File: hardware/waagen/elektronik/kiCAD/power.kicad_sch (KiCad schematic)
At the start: 7 parts, among them U2 MCP1700-3302E_TO92

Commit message: fues added and small movements
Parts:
- added F1: Polyfuse 500mA, Resistor_SMD:R_1206_3216Metric_Pad1.30x1.75mm_HandSolder, symbol Device:Polyfuse
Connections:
- net +9V: now also F1.1; no longer C7.1, U2.2 (VI)
- new net: C7.1, F1.2, U2.2 (VI)
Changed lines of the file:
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@@
 (kicad_sch (version 20211123) (generator eeschema)
   (paper "A4")
+  (junction (at 111.76 91.44) (diameter 0) (color 0 0 0 0)
+  )
+  (junction (at 93.98 91.44) (diameter 0) (color 0 0 0 0)
+  )
   (junction (at 138.43 91.44) (diameter 0) (color 0 0 0 0)
   )
-  (junction (at 111.76 91.44) (diameter 0) (color 0 0 0 0)
-  )
-  (junction (at 93.98 91.44) (diameter 0) (color 0 0 0 0)
+  (junction (at 148.59 91.44) (diameter 0) (color 0 0 0 0)
   )
   (junction (at 102.87 91.44) (diameter 0) (color 0 0 0 0)
@@
     (stroke (width 0) (type default) (color 0 0 0 0))
   )
+  (wire (pts (xy 219.71 105.41) (xy 219.71 106.68))
+    (stroke (width 0) (type default) (color 0 0 0 0))
+  )
+  (wire (pts (xy 138.43 99.06) (xy 138.43 102.87))
+    (stroke (width 0) (type default) (color 0 0 0 0))
+  )
+  (wire (pts (xy 125.73 99.06) (xy 125.73 102.87))
+    (stroke (width 0) (type default) (color 0 0 0 0))
+  )
   (wire (pts (xy 133.35 91.44) (xy 138.43 91.44))
     (stroke (width 0) (type default) (color 0 0 0 0))
   )
-  (wire (pts (xy 219.71 105.41) (xy 219.71 106.68))
-    (stroke (width 0) (type default) (color 0 0 0 0))
-  )
-  (wire (pts (xy 138.43 99.06) (xy 138.43 102.87))
-    (stroke (width 0) (type default) (color 0 0 0 0))
-  )
-  (wire (pts (xy 125.73 99.06) (xy 125.73 102.87))
-    (stroke (width 0) (type default) (color 0 0 0 0))
-  )
   (wire (pts (xy 138.43 91.44) (xy 148.59 91.44))
     (stroke (width 0) (type default) (color 0 0 0 0))
@@
     (stroke (width 0) (type default) (color 0 0 0 0))
   )
+  (wire (pts (xy 148.59 91.44) (xy 148.59 99.06))
+    (stroke (width 0) (type default) (color 0 0 0 0))
+  )
   (wire (pts (xy 148.59 91.44) (xy 148.59 90.17))
     (stroke (width 0) (type default) (color 0 0 0 0))
   )
-  (wire (pts (xy 179.07 93.98) (xy 179.07 97.79))
+  (wire (pts (xy 189.23 95.25) (xy 189.23 99.06))
     (stroke (width 0) (type default) (color 0 0 0 0))
   )
@@
     (stroke (width 0) (type default) (color 0 0 0 0))
   )
+  (wire (pts (xy 177.8 93.98) (xy 177.8 99.06))
+    (stroke (width 0) (type default) (color 0 0 0 0))
+  )
   (wire (pts (xy 93.98 99.06) (xy 93.98 102.87))
     (stroke (width 0) (type default) (color 0 0 0 0))
   )
-  (wire (pts (xy 168.91 93.98) (xy 168.91 97.79))
-    (stroke (width 0) (type default) (color 0 0 0 0))
-  )
   (wire (pts (xy 219.71 87.63) (xy 219.71 88.9))
     (stroke (width 0) (type default) (color 0 0 0 0))
@@
     (stroke (width 0) (type default) (color 0 0 0 0))
   )
+  (wire (pts (xy 148.59 80.01) (xy 148.59 82.55))
+    (stroke (width 0) (type default) (color 0 0 0 0))
+  )
   (wire (pts (xy 111.76 91.44) (xy 118.11 91.44))
     (stroke (width 0) (type default) (color 0 0 0 0))
   )
-  (text "For KiCAD ERC only" (at 166.37 86.36 0)
+  (text "For KiCAD ERC only" (at 176.53 87.63 0)
     (effects (font (size 1.27 1.27)) (justify left bottom))
   )
@@
     (pin "1")
   )
-  (symbol (lib_id "power:GND") (at 179.07 97.79 0) (unit 1)
-    (in_bom yes) (on_board yes) (fields_autoplaced)
-    (property "Reference" "#PWR018" (id 0) (at 179.07 104.14 0)
-      (effects (font (size 1.27 1.27)) hide)
-    )
-    (property "Value" "GND" (id 1) (at 179.07 102.87 0))
-    (property "Footprint" "" (id 2) (at 179.07 97.79 0)
-      (effects (font (size 1.27 1.27)) hide)
-    )
-    (property "Datasheet" "" (id 3) (at 179.07 97.79 0)
-      (effects (font (size 1.27 1.27)) hide)
-    )
-    (pin "1")
-  )
-  (symbol (lib_id "power:+9V") (at 148.59 90.17 0) (unit 1)
-    (in_bom yes) (on_board yes) (fields_autoplaced)
-    (property "Reference" "#PWR016" (id 0) (at 148.59 93.98 0)
-      (effects (font (size 1.27 1.27)) hide)
-    )
-    (property "Value" "+9V" (id 1) (at 148.59 85.09 0))
-    (property "Footprint" "" (id 2) (at 148.59 90.17 0)
-      (effects (font (size 1.27 1.27)) hide)
-    )
-    (property "Datasheet" "" (id 3) (at 148.59 90.17 0)
-      (effects (font (size 1.27 1.27)) hide)
-    )
-    (pin "1")
+  (symbol (lib_id "power:GND") (at 189.23 99.06 0) (unit 1)
+    (in_bom yes) (on_board yes) (fields_autoplaced)
+    (property "Reference" "#PWR018" (id 0) (at 189.23 105.41 0)
+      (effects (font (size 1.27 1.27)) hide)
+    )
+    (property "Value" "GND" (id 1) (at 189.23 104.14 0))
+    (property "Footprint" "" (id 2) (at 189.23 99.06 0)
+      (effects (font (size 1.27 1.27)) hide)
+    )
+    (property "Datasheet" "" (id 3) (at 189.23 99.06 0)
+      (effects (font (size 1.27 1.27)) hide)
+    )
+    (pin "1")
+  )
+  (symbol (lib_id "power:+9V") (at 148.59 80.01 0) (unit 1)
+    (in_bom yes) (on_board yes) (fields_autoplaced)
+    (property "Reference" "#PWR016" (id 0) (at 148.59 83.82 0)
+      (effects (font (size 1.27 1.27)) hide)
+    )
+    (property "Value" "+9V" (id 1) (at 148.59 74.93 0))
+    (property "Footprint" "" (id 2) (at 148.59 80.01 0)
+      (effects (font (size 1.27 1.27)) hide)
+    )
+    (property "Datasheet" "" (id 3) (at 148.59 80.01 0)
+      (effects (font (size 1.27 1.27)) hide)
+    )
+    (pin "1")
+  )
+  (symbol (lib_id "Device:Polyfuse") (at 148.59 86.36 0) (unit 1)
+    (in_bom yes) (on_board yes) (fields_autoplaced)
+    (property "Reference" "F1" (id 0) (at 151.13 85.0899 0)
+      (effects (font (size 1.27 1.27)) (justify left))
+    )
+    (property "Value" "Polyfuse 500mA" (id 1) (at 151.13 87.6299 0)
+      (effects (font (size 1.27 1.27)) (justify left))
+    )
+    (property "Footprint" "Resistor_SMD:R_1206_3216Metric_Pad1.30x1.75mm_HandSolder" (id 2) (at 149.86 91.44 0)
+      (effects (font (size 1.27 1.27)) (justify left) hide)
+    )
+    (property "Datasheet" "~" (id 3) (at 148.59 86.36 0)
+      (effects (font (size 1.27 1.27)) hide)
+    )
+    (pin "1")
+    (pin "2")
   )
   (symbol (lib_id "power:GND") (at 138.43 102.87 0) (unit 1)
@@
     (pin "2")
   )
-  (symbol (lib_id "power:+9V") (at 168.91 93.98 0) (unit 1)
-    (in_bom yes) (on_board yes) (fields_autoplaced)
-    (property "Reference" "#PWR017" (id 0) (at 168.91 97.79 0)
-      (effects (font (size 1.27 1.27)) hide)
-    )
-    (property "Value" "+9V" (id 1) (at 168.91 88.9 0))
-    (property "Footprint" "" (id 2) (at 168.91 93.98 0)
-      (effects (font (size 1.27 1.27)) hide)
-    )
-    (property "Datasheet" "" (id 3) (at 168.91 93.98 0)
-      (effects (font (size 1.27 1.27)) hide)
-    )
-    (pin "1")
-  )
-  (symbol (lib_id "power:PWR_FLAG") (at 179.07 93.98 0) (unit 1)
-    (in_bom yes) (on_board yes) (fields_autoplaced)
-    (property "Reference" "#FLG02" (id 0) (at 179.07 92.075 0)
-      (effects (font (size 1.27 1.27)) hide)
-    )
-    (property "Value" "PWR_FLAG" (id 1) (at 179.07 88.9 0))
-    (property "Footprint" "" (id 2) (at 179.07 93.98 0)
-      (effects (font (size 1.27 1.27)) hide)
-    )
-    (property "Datasheet" "~" (id 3) (at 179.07 93.98 0)
+  (symbol (lib_id "power:PWR_FLAG") (at 189.23 95.25 0) (unit 1)
+    (in_bom yes) (on_board yes) (fields_autoplaced)
+    (property "Reference" "#FLG02" (id 0) (at 189.23 93.345 0)
+      (effects (font (size 1.27 1.27)) hide)
+    )
+    (property "Value" "PWR_FLAG" (id 1) (at 189.23 90.17 0))
+    (property "Footprint" "" (id 2) (at 189.23 95.25 0)
+      (effects (font (size 1.27 1.27)) hide)
+    )
+    (property "Datasheet" "~" (id 3) (at 189.23 95.25 0)
       (effects (font (size 1.27 1.27)) hide)
     )
@@
     (pin "1")
   )
+  (symbol (lib_id "power:PWR_FLAG") (at 177.8 99.06 180) (unit 1)
+    (in_bom yes) (on_board yes) (fields_autoplaced)
+    (property "Reference" "#FLG03" (id 0) (at 177.8 100.965 0)
+      (effects (font (size 1.27 1.27)) hide)
+    )
+    (property "Value" "PWR_FLAG" (id 1) (at 177.8 104.14 0))
+    (property "Footprint" "" (id 2) (at 177.8 99.06 0)
+      (effects (font (size 1.27 1.27)) hide)
+    )
+    (property "Datasheet" "~" (id 3) (at 177.8 99.06 0)
+      (effects (font (size 1.27 1.27)) hide)
+    )
+    (pin "1")
+  )
   (symbol (lib_id "power:GND") (at 93.98 102.87 0) (unit 1)
     (in_bom yes) (on_board yes) (fields_autoplaced)
@@
     (pin "2")
   )
-  (symbol (lib_id "power:PWR_FLAG") (at 168.91 97.79 180) (unit 1)
-    (in_bom yes) (on_board yes) (fields_autoplaced)
-    (property "Reference" "#FLG01" (id 0) (at 168.91 99.695 0)
-      (effects (font (size 1.27 1.27)) hide)
-    )
-    (property "Value" "PWR_FLAG" (id 1) (at 168.91 102.87 0))
-    (property "Footprint" "" (id 2) (at 168.91 97.79 0)
-      (effects (font (size 1.27 1.27)) hide)
-    )
-    (property "Datasheet" "~" (id 3) (at 168.91 97.79 0)
-      (effects (font (size 1.27 1.27)) hide)
-    )
+  (symbol (lib_id "power:+9V") (at 177.8 93.98 0) (unit 1)
+    (in_bom yes) (on_board yes) (fields_autoplaced)
+    (property "Reference" "#PWR017" (id 0) (at 177.8 97.79 0)
+      (effects (font (size 1.27 1.27)) hide)
+    )
+    (property "Value" "+9V" (id 1) (at 177.8 88.9 0))
+    (property "Footprint" "" (id 2) (at 177.8 93.98 0)
+      (effects (font (size 1.27 1.27)) hide)
+    )
+    (property "Datasheet" "" (id 3) (at 177.8 93.98 0)
+      (effects (font (size 1.27 1.27)) hide)
+    )
+    (pin "1")
+  )
+  (symbol (lib_id "power:PWR_FLAG") (at 148.59 99.06 180) (unit 1)
+    (in_bom yes) (on_board yes) (fields_autoplaced)
+    (property "Reference" "#FLG01" (id 0) (at 148.59 100.965 0)
+      (effects (font (size 1.27 1.27)) hide)
+    )
+    (property "Value" "PWR_FLAG" (id 1) (at 148.59 104.14 0))
+    (property "Footprint" "" (id 2) (at 148.59 99.06 0)
+      (effects (font (size 1.27 1.27)) hide)
+    )
+    (property "Datasheet" "~" (id 3) (at 148.59 99.06 0)
+      (effects (font (size 1.27 1.27)) hide)
+    )

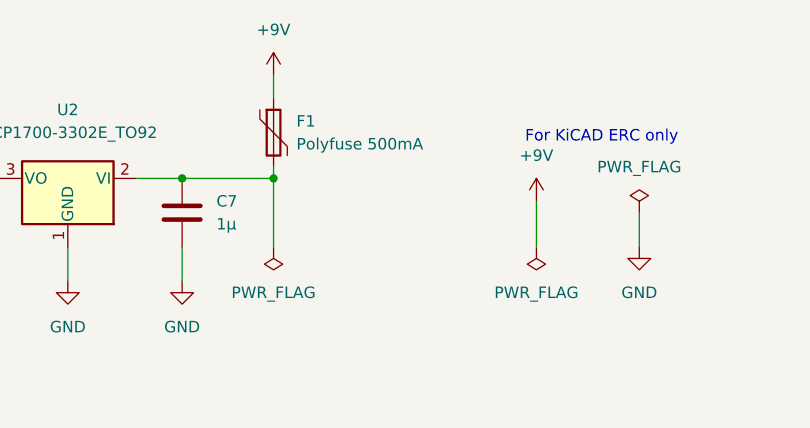
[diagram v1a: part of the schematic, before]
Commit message: CAN SPI CS pin corrected and PCB optimisations.
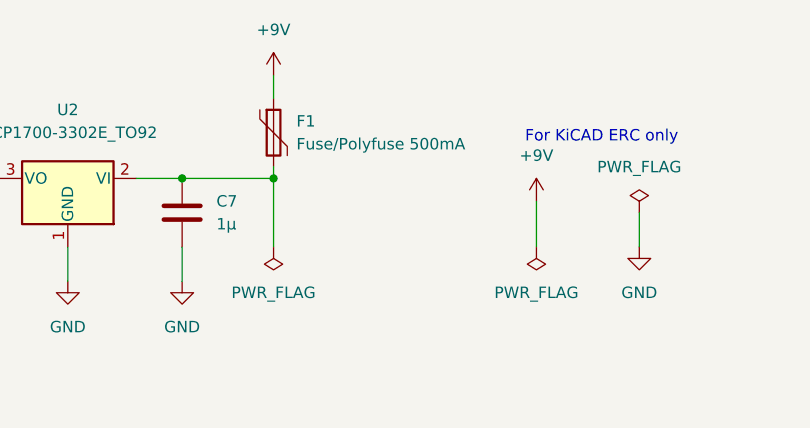
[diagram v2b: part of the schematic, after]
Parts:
- F1: value Polyfuse 500mA -> Fuse/Polyfuse 500mA; footprint Resistor_SMD:R_1206_3216Metric_Pad1.30x1.75mm_HandSolder -> Fuse:Fuse_2512_6332Metric_Pad1.52x3.35mm_HandSolder
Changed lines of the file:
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@@
       (effects (font (size 1.27 1.27)) (justify left))
     )
-    (property "Value" "Polyfuse 500mA" (id 1) (at 151.13 87.6299 0)
+    (property "Value" "Fuse/Polyfuse 500mA" (id 1) (at 151.13 87.6299 0)
       (effects (font (size 1.27 1.27)) (justify left))
     )
-    (property "Footprint" "Resistor_SMD:R_1206_3216Metric_Pad1.30x1.75mm_HandSolder" (id 2) (at 149.86 91.44 0)
+    (property "Footprint" "Fuse:Fuse_2512_6332Metric_Pad1.52x3.35mm_HandSolder" (id 2) (at 149.86 91.44 0)
       (effects (font (size 1.27 1.27)) (justify left) hide)
     )

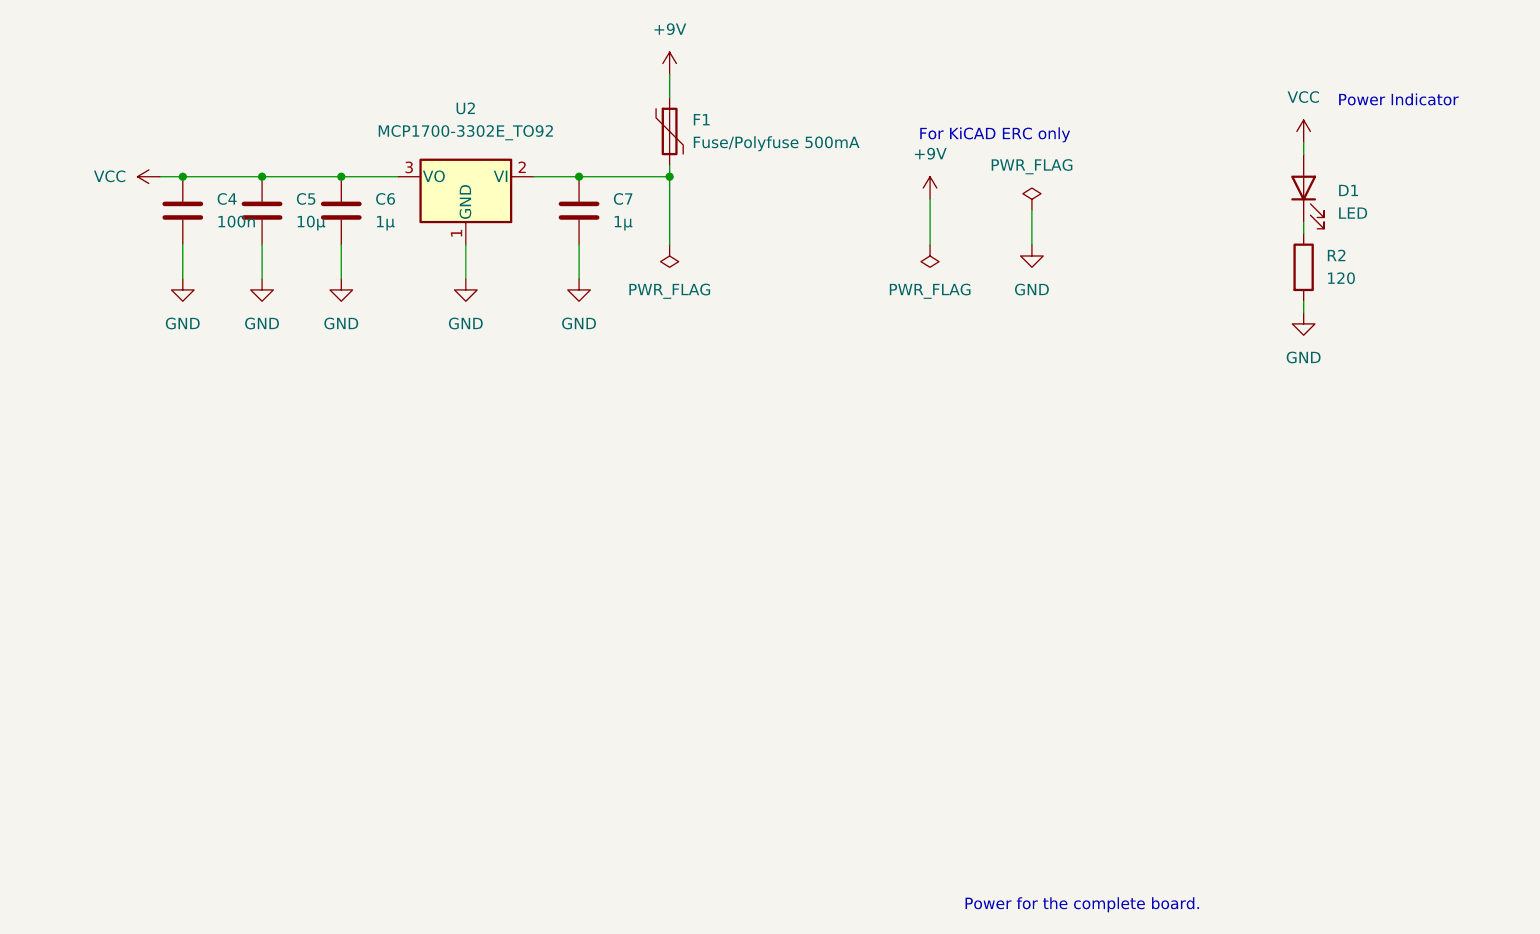
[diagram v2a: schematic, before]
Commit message: second LDO for eink added
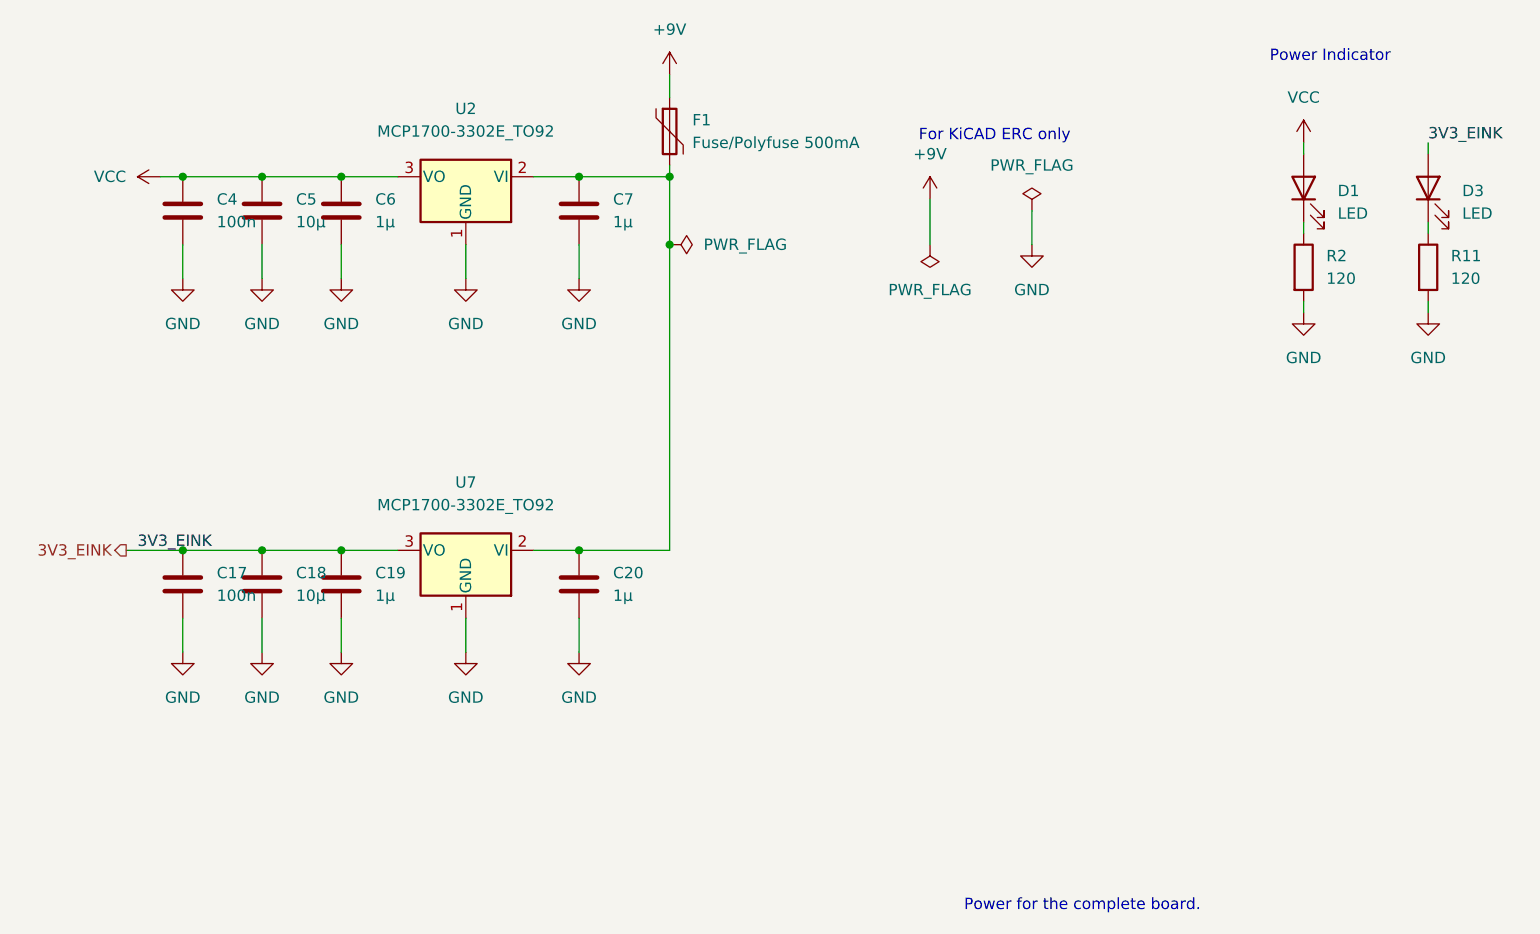
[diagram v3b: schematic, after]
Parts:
- added C17: 100n, Capacitor_SMD:C_1206_3216Metric_Pad1.33x1.80mm_HandSolder, symbol Device:C
- added C18: 10µ, Capacitor_SMD:C_1206_3216Metric_Pad1.33x1.80mm_HandSolder, symbol Device:C
- added C19, C20: 1µ, Capacitor_SMD:C_1206_3216Metric_Pad1.33x1.80mm_HandSolder, symbol Device:C
- added D3: LED, LED_SMD:LED_1206_3216Metric_Pad1.42x1.75mm_HandSolder, symbol Device:LED
- added R11: 120, Resistor_SMD:R_1206_3216Metric_Pad1.30x1.75mm_HandSolder, symbol Device:R
- added U7: MCP1700-3302E_TO92, Package_TO_SOT_THT:TO-92_Inline, symbol Regulator_Linear:MCP1700-3302E_TO92
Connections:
- net GND: now also C17.2, C18.2, C19.2, C20.2, R11.2, U7.1 (GND)
- net at C7.1, F1.2, U2.2 (VI): now also C20.1, U7.2 (VI)
- new net: D3.1 (K), R11.1
- new net 3V3_EINK: C17.1, C18.1, C19.1, D3.2 (A), U7.3 (VO)
